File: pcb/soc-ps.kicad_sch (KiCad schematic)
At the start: 1 part, among them U1 XC7Z020CLG484

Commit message: hierarchy and cleaning
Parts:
- removed U1: XC7Z020CLG484, Package_BGA:Xilinx_CLG484_CLG485, symbol library:XC7Z020CLG484
- added U1: XC7Z020CLG484, Package_BGA:Xilinx_CLG484_CLG485, symbol library:XC7Z020CLG484

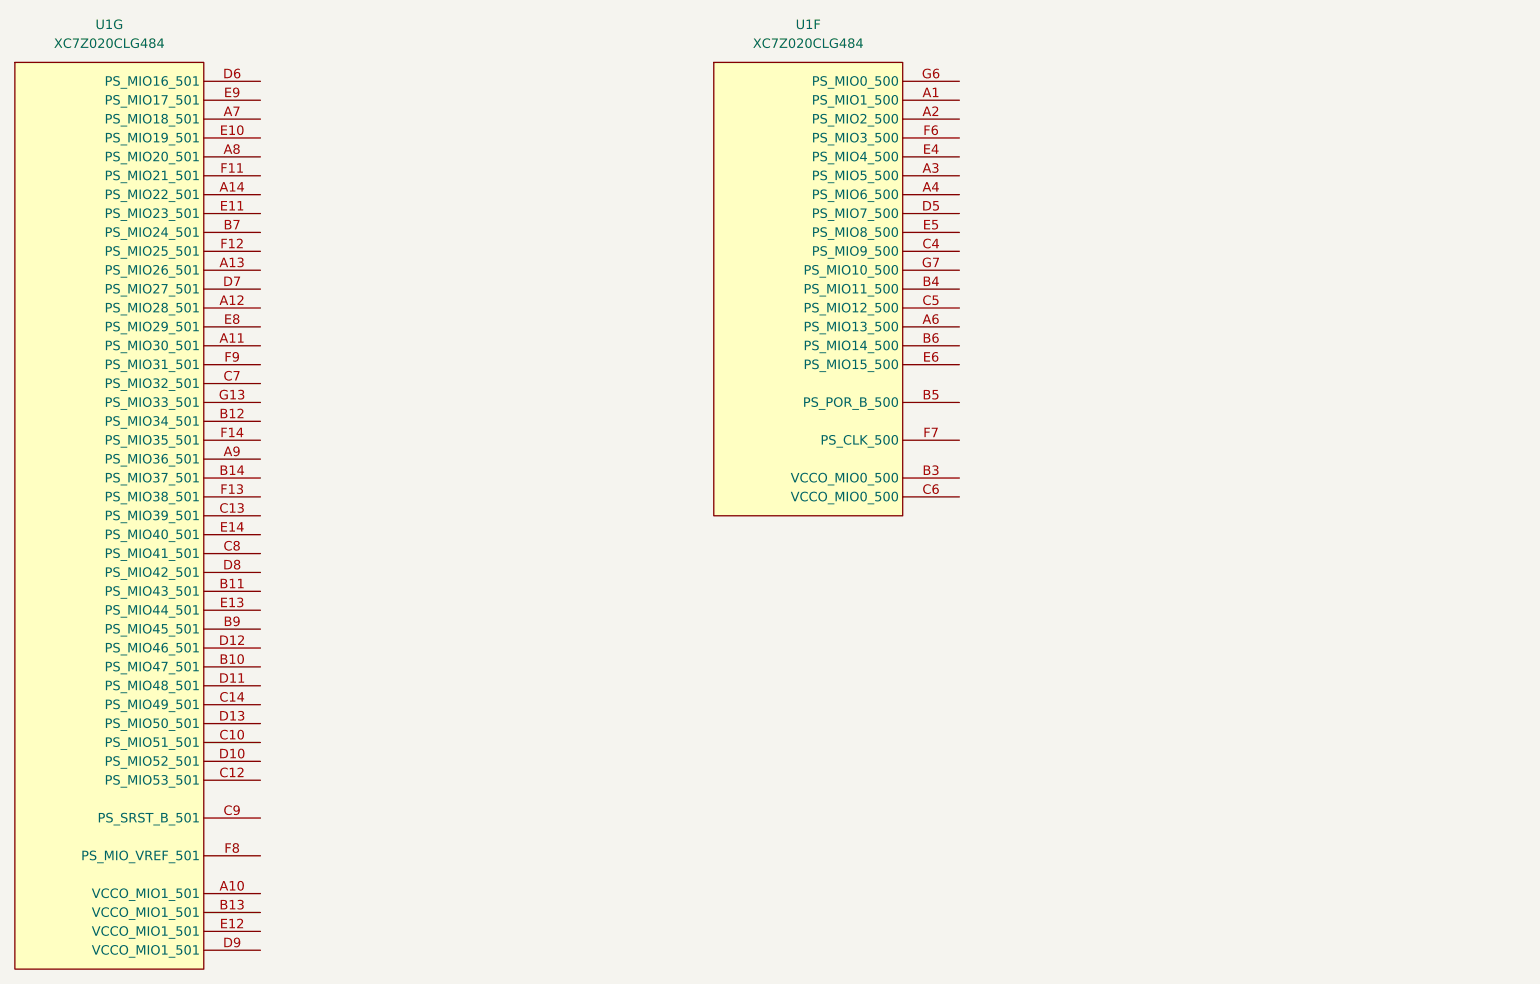
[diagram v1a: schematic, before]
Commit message: schematic structure, added qspi flash, pinout defs. mostly work on PS pinouts, defining comms. buses, still need to choose dram part, phys, camera/bus, power supply etc
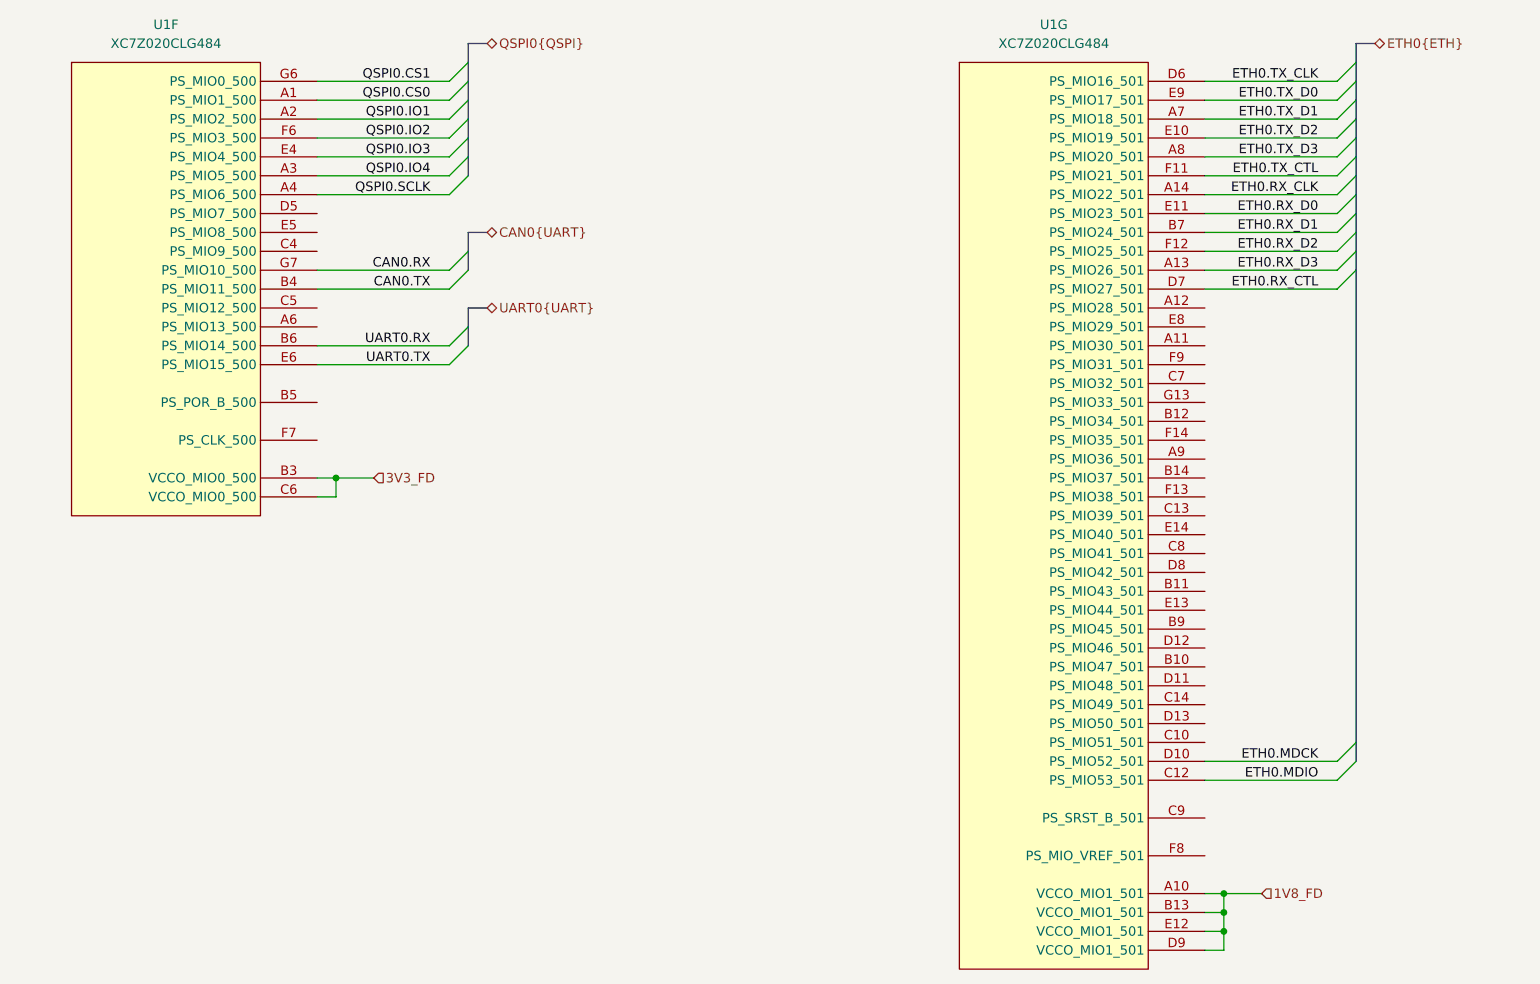
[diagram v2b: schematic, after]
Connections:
- net QSPI0.CS0: now reaches U1.A1 (PS_MIO1_500)
- net QSPI0.IO1: now reaches U1.A2 (PS_MIO2_500)
- net QSPI0.IO4: now reaches U1.A3 (PS_MIO5_500)
- net QSPI0.SCLK: now reaches U1.A4 (PS_MIO6_500)
- net 3V3_FD: now reaches U1.B3 (VCCO_MIO0_500)
- net 3V3_FD: now also U1.C6 (VCCO_MIO0_500)
- net CAN0.TX: now reaches U1.B4 (PS_MIO11_500)
- net UART0.RX: now reaches U1.B6 (PS_MIO14_500)
- net QSPI0.IO3: now reaches U1.E4 (PS_MIO4_500)
- net UART0.TX: now reaches U1.E6 (PS_MIO15_500)
- net QSPI0.IO2: now reaches U1.F6 (PS_MIO3_500)
- net QSPI0.CS1: now reaches U1.G6 (PS_MIO0_500)
- net CAN0.RX: now reaches U1.G7 (PS_MIO10_500)
- net 1V8_FD: now reaches U1.A10 (VCCO_MIO1_501)
- net 1V8_FD: now also U1.B13 (VCCO_MIO1_501), U1.D9 (VCCO_MIO1_501), U1.E12 (VCCO_MIO1_501)
- net ETH0.RX_D3: now reaches U1.A13 (PS_MIO26_501)
- net ETH0.RX_CLK: now reaches U1.A14 (PS_MIO22_501)
- net ETH0.TX_D1: now reaches U1.A7 (PS_MIO18_501)
- net ETH0.TX_D3: now reaches U1.A8 (PS_MIO20_501)
- net ETH0.RX_D1: now reaches U1.B7 (PS_MIO24_501)
- net ETH0.MDIO: now reaches U1.C12 (PS_MIO53_501)
- net ETH0.MDCK: now reaches U1.D10 (PS_MIO52_501)
- net ETH0.TX_CLK: now reaches U1.D6 (PS_MIO16_501)
- net ETH0.RX_CTL: now reaches U1.D7 (PS_MIO27_501)
- net ETH0.TX_D2: now reaches U1.E10 (PS_MIO19_501)
- net ETH0.RX_D0: now reaches U1.E11 (PS_MIO23_501)
- net ETH0.TX_D0: now reaches U1.E9 (PS_MIO17_501)
- net ETH0.TX_CTL: now reaches U1.F11 (PS_MIO21_501)
- net ETH0.RX_D2: now reaches U1.F12 (PS_MIO25_501)
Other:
- title: (none) -> CUTIE-CITRUS
- moved on the sheet: U1F, U1G

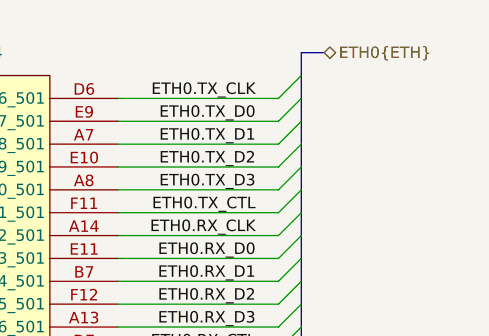
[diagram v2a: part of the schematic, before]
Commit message: edits to eth0 protocol names / bus aliases
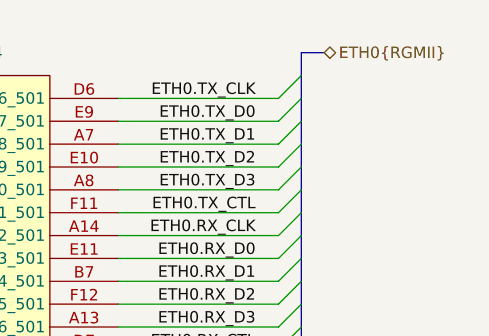
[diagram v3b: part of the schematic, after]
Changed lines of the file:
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@@
 		(members "P" "N")
 	)
-	(bus_alias "ETH"
+	(bus_alias "I2C"
+		(members "SCL" "SDA")
+	)
+	(bus_alias "QSPI"
+		(members "CS1" "CS0" "IO0" "IO1" "IO2" "IO3" "SCLK")
+	)
+	(bus_alias "RGMII"
 		(members "TX_CLK" "TX_D0" "TX_D1" "TX_D2" "TX_D3" "TX_CTL" "RX_CLK" "RX_D0"
 			"RX_D1" "RX_D2" "RX_D3" "RX_CTL" "MDCK" "MDIO"
 		)
-	)
-	(bus_alias "I2C"
-		(members "SCL" "SDA")
-	)
-	(bus_alias "QSPI"
-		(members "CS1" "CS0" "IO0" "IO1" "IO2" "IO3" "SCLK")
 	)
 	(bus_alias "UART"
@@
 		)
 	)
-	(hierarchical_label "ETH0{ETH}"
+	(hierarchical_label "ETH0{RGMII}"
 		(shape bidirectional)
 		(at 203.2 22.86 0)
